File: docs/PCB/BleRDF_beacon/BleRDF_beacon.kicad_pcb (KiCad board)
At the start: 2 copper layers, 47 x 36 mm, 11 parts, among them J1 Conn_01x02, J2 Conn_01x02, J3 Conn_01x02, J4 Conn_01x02, U1 XIAO-ESP32-C6

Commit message: Update PCB wiring and add 3D case models
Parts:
- moved J4 20.6 mm to (58.0, 56.0)
- moved R3 6.13 mm to (63.0, 61.0), turned to 180 degrees
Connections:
- R3 pad 1: Net-(U1-GPIO20/D9/MISO) -> Net-(U1-GPIO17/D7/RX)
- U1 pad 10: Net-(U1-GPIO20/D9/MISO) -> unconnected-(U1-GPIO20/D9/MISO-Pad10)_1
- U1 pad 8: unconnected-(U1-GPIO17/D7/RX-Pad8)_1 -> Net-(U1-GPIO17/D7/RX)
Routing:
- net Net-(U1-GPIO20/D9/MISO): track 15.8 -> 0.00 mm
- net Net-(U1-GPIO17/D7/RX): track 0.00 -> 7.69 mm
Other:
- outline, holes or cut-outs redrawn
- board text added: "BleRDF Beacon v1.0"
- board text removed: "BleRDF Beacon"
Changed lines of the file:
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@@
 	(net 4 "Net-(U1-GPIO0{slash}A0{slash}D0)")
 	(net 5 "Net-(J2-Pin_2)")
-	(net 6 "Net-(U1-GPIO20{slash}D9{slash}MISO)")
+	(net 6 "Net-(U1-GPIO17{slash}D7{slash}RX)")
 	(net 7 "unconnected-(U1-GPIO19{slash}D8{slash}SCK-Pad9)")
 	(net 8 "unconnected-(U1-GPIO2{slash}A2{slash}D2-Pad3)")
@@
 	(net 13 "unconnected-(U1-GPIO22{slash}D4{slash}SDA-Pad5)")
 	(net 14 "unconnected-(U1-GPIO21{slash}D3-Pad4)_1")
-	(net 15 "unconnected-(U1-GPIO17{slash}D7{slash}RX-Pad8)")
+	(net 15 "unconnected-(U1-GPIO20{slash}D9{slash}MISO-Pad10)")
 	(net 16 "unconnected-(U1-GPIO18{slash}D10{slash}MOSI-Pad11)_1")
 	(net 17 "unconnected-(U1-GPIO19{slash}D8{slash}SCK-Pad9)_1")
@@
 	(net 23 "unconnected-(U1-GPIO23{slash}D5{slash}SCL-Pad6)_1")
 	(net 24 "unconnected-(U1-GPIO1{slash}A1{slash}D1-Pad2)_1")
-	(net 25 "unconnected-(U1-GPIO17{slash}D7{slash}RX-Pad8)_1")
+	(net 25 "unconnected-(U1-GPIO20{slash}D9{slash}MISO-Pad10)_1")
 	(net 26 "unconnected-(U1-GPIO22{slash}D4{slash}SDA-Pad5)_1")
 	(net 27 "VCC")
@@
 		(tags "CONN DEV")
 		(property "Reference" "F1"
-			(at -3 0.9 90)
+			(at 1.1 1.9 90)
 			(layer "F.SilkS")
 			(effects
@@
 		)
 		(fp_text user "${REFERENCE}"
-			(at 5 -0.91 90)
+			(at 1.25 0 90)
 			(layer "F.Fab")
 			(effects
@@
 	(footprint "Connector_JST:JST_XH_B2B-XH-A_1x02_P2.50mm_Vertical"
 		(layer "F.Cu")
-		(at 59.5 76.5 180)
+		(at 58 56 180)
 		(descr "JST XH series connector, B2B-XH-A (http://www.jst-mfg.com/product/pdf/eng/eXH.pdf), generated with kicad-footprint-generator")
 		(tags "connector JST XH vertical")
 		(property "Reference" "J4"
-			(at -1.5 5 0)
+			(at -4 -0.6 0)
 			(layer "F.SilkS")
 			(effects
@@
 	(footprint "Resistor_THT:R_Axial_DIN0204_L3.6mm_D1.6mm_P7.62mm_Horizontal"
 		(layer "F.Cu")
-		(at 57.5 63.69 -90)
+		(at 63.01 61 180)
 		(descr "Resistor, Axial_DIN0204 series, Axial, Horizontal, pin pitch=7.62mm, 0.167W, length*diameter=3.6*1.6mm^2, http://cdn-reichelt.de/documents/datenblatt/B400/1_4W%23YAG.pdf")
 		(tags "Resistor Axial_DIN0204 series Axial Horizontal pin pitch 7.62mm 0.167W length 3.6mm diameter 1.6mm")
 		(property "Reference" "R3"
-			(at 3.81 0 90)
+			(at 3.81 0 0)
 			(layer "F.SilkS")
 			(effects
@@
 		)
 		(property "Value" "1k"
-			(at 3.81 1.92 90)
+			(at 3.81 1.92 0)
 			(layer "F.Fab")
 			(hide yes)
@@
 		)
 		(property "Datasheet" "~"
-			(at 0 0 90)
+			(at 0 0 0)
 			(layer "F.Fab")
 			(hide yes)
@@
 		)
 		(property "Description" "Resistor"
-			(at 0 0 90)
+			(at 0 0 0)
 			(layer "F.Fab")
 			(hide yes)
@@
 		(attr through_hole)
 		(fp_line
-			(start 0.94 0)
-			(end 1.89 0)
+			(start 6.68 0)
+			(end 5.73 0)
 			(stroke
 				(width 0.12)
@@
 		)
 		(fp_line
-			(start 6.68 0)
-			(end 5.73 0)
+			(start 0.94 0)
+			(end 1.89 0)
 			(stroke
 				(width 0.12)
@@
 		)
 		(fp_line
-			(start 0 0)
-			(end 2.01 0)
+			(start 7.62 0)
+			(end 5.61 0)
 			(stroke
 				(width 0.1)
@@
 		)
 		(fp_line
-			(start 7.62 0)
-			(end 5.61 0)
+			(start 0 0)
+			(end 2.01 0)
 			(stroke
 				(width 0.1)
@@
 		)
 		(fp_text user "${REFERENCE}"
-			(at 3.81 0 90)
+			(at 3.81 0 0)
 			(layer "F.Fab")
 			(effects
@@
 		)
 		(pad "1" thru_hole circle
-			(at 0 0 270)
+			(at 0 0 180)
 			(size 1.4 1.4)
 			(drill 0.7)
 			(layers "*.Cu" "*.Mask")
 			(remove_unused_layers no)
-			(net 6 "Net-(U1-GPIO20{slash}D9{slash}MISO)")
+			(net 6 "Net-(U1-GPIO17{slash}D7{slash}RX)")
 			(pintype "passive")
 		)
 		(pad "2" thru_hole circle
-			(at 7.62 0 270)
+			(at 7.62 0 180)
 			(size 1.4 1.4)
 			(drill 0.7)
@@
 			(layers "*.Cu" "*.Mask")
 			(remove_unused_layers no)
-			(net 15 "unconnected-(U1-GPIO17{slash}D7{slash}RX-Pad8)")
+			(net 6 "Net-(U1-GPIO17{slash}D7{slash}RX)")
 			(pinfunction "GPIO17/D7/RX")
-			(pintype "passive+no_connect")
+			(pintype "passive")
 		)
 		(pad "8" smd roundrect
@@
 			(layers "F.Cu" "F.Mask")
 			(roundrect_rratio 0.1)
-			(net 25 "unconnected-(U1-GPIO17{slash}D7{slash}RX-Pad8)_1")
+			(net 6 "Net-(U1-GPIO17{slash}D7{slash}RX)")
 			(pinfunction "GPIO17/D7/RX")
-			(pintype "passive+no_connect")
+			(pintype "passive")
 			(thermal_bridge_angle 45)
 		)
@@
 			(layers "*.Cu" "*.Mask")
 			(remove_unused_layers no)
-			(net 6 "Net-(U1-GPIO20{slash}D9{slash}MISO)")
+			(net 15 "unconnected-(U1-GPIO20{slash}D9{slash}MISO-Pad10)")
 			(pinfunction "GPIO20/D9/MISO")
-			(pintype "passive")
+			(pintype "passive+no_connect")
 		)
 		(pad "10" smd roundrect
@@
 			(layers "F.Cu" "F.Mask")
 			(roundrect_rratio 0.1)
-			(net 6 "Net-(U1-GPIO20{slash}D9{slash}MISO)")
+			(net 25 "unconnected-(U1-GPIO20{slash}D9{slash}MISO-Pad10)_1")
 			(pinfunction "GPIO20/D9/MISO")
-			(pintype "passive")
+			(pintype "passive+no_connect")
 			(thermal_bridge_angle 45)
 		)
@@
 		(tags "connector JST XH vertical")
 		(property "Reference" "J3"
-			(at 5 -4.25 90)
+			(at 1.8 -3.6 90)
 			(layer "F.SilkS")
 			(effects
@@
 		(embedded_fonts no)
 	)
-	(gr_rect
-		(start 50 50)
-		(end 97 86)
+	(gr_line
+		(start 50 84)
+		(end 52 86)
+		(stroke
+			(width 0.2)
+			(type default)
+		)
+		(layer "Edge.Cuts")
+	)
+	(gr_line
+		(start 52 86)
+		(end 95 86)
+		(stroke
+			(width 0.2)
+			(type default)
+		)
+		(layer "Edge.Cuts")
+	)
+	(gr_line
+		(start 95 86)
+		(end 97 84)
+		(stroke
+			(width 0.2)
+			(type default)
+		)
+		(layer "Edge.Cuts")
+	)
+	(gr_line
+		(start 95 50)
+		(end 52 50)
+		(stroke
+			(width 0.2)
+			(type default)
+		)
+		(layer "Edge.Cuts")
+	)
+	(gr_line
+		(start 50 52)
+		(end 50 84)
+		(stroke
+			(width 0.2)
+			(type default)
+		)
+		(layer "Edge.Cuts")
+	)
+	(gr_line
+		(start 97 52)
+		(end 95 50)
+		(stroke
+			(width 0.2)
+			(type default)
+		)
+		(layer "Edge.Cuts")
+	)
+	(gr_line
+		(start 52 50)
+		(end 50 52)
+		(stroke
+			(width 0.2)
+			(type default)
+		)
+		(layer "Edge.Cuts")
+	)
+	(gr_line
+		(start 97 84)
+		(end 97 52)
 		(stroke
-			(width 0.05)
+			(width 0.2)
 			(type default)
 		)
-		(fill no)
 		(layer "Edge.Cuts")
 	)
-	(gr_text "BleRDF\nBeacon"
-		(at 51.25 84.25 0)
-		(layer "F.SilkS")
+	(gr_text "BleRDF\nBeacon v1.0"
+		(at 95.3 55.9 0)
+		(layer "B.SilkS")
 		(effects
 			(font
@@
 				(thickness 0.2)
 			)
-			(justify left bottom)
+			(justify left bottom mirror)
 		)
 	)
@@
 	)
 	(segment
-		(start 57.5 63.69)
-		(end 59.94 63.69)
-		(width 0.5)
-		(layer "F.Cu")
-		(net 6)
-	)
-	(segment
-		(start 61 64.75)
-		(end 61 71)
-		(width 0.5)
-		(layer "F.Cu")
-		(net 6)
-	)
-	(segment
-		(start 62.39 72.39)
-		(end 66.04 72.39)
-		(width 0.5)
-		(layer "F.Cu")
-		(net 6)
-	)
-	(segment
-		(start 59.94 63.69)
-		(end 61 64.75)
+		(start 63.01 64.28)
+		(end 66.04 67.31)
 		(width 0.5)
 		(layer "F.Cu")
@@
 	)
 	(segment
-		(start 61 71)
-		(end 62.39 72.39)
+		(start 63.01 61)
+		(end 63.01 64.28)
 		(width 0.5)
 		(layer "F.Cu")
@@
 		(width 0.5)
 		(layer "B.Cu")
-		(net 15)
+		(net 6)
 	)
 	(segment
@@
 	(segment
 		(start 63.01 80.01)
-		(end 66.04 80.01)
+		(end 59.5 76.5)
 		(width 0.5)
-		(layer "F.Cu")
+		(layer "B.Cu")
 		(net 28)
 	)
 	(segment
-		(start 59.5 76.5)
+		(start 66.04 80.01)
 		(end 63.01 80.01)
 		(width 0.5)
-		(layer "F.Cu")
+		(layer "B.Cu")
 		(net 28)
 	)
 	(segment
-		(start 57.5 71.31)
-		(end 57.5 76)
+		(start 55.5 56)
+		(end 55.5 60.89)
 		(width 0.5)
 		(layer "F.Cu")
@@
 	)
 	(segment
-		(start 57.5 76)
-		(end 57 76.5)
+		(start 55.5 60.89)
+		(end 55.39 61)
 		(width 0.5)
 		(layer "F.Cu")

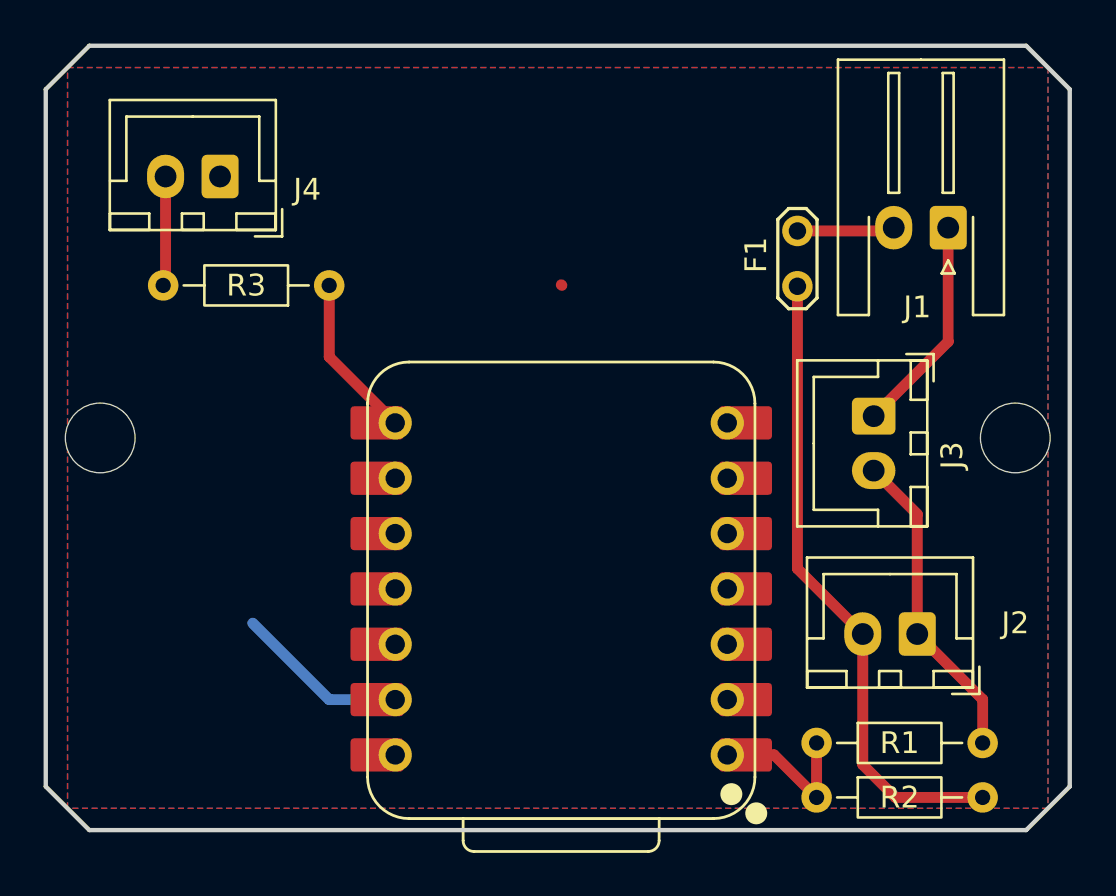
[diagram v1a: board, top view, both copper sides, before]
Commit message: Update 3D cases and pcb,hardware documentation
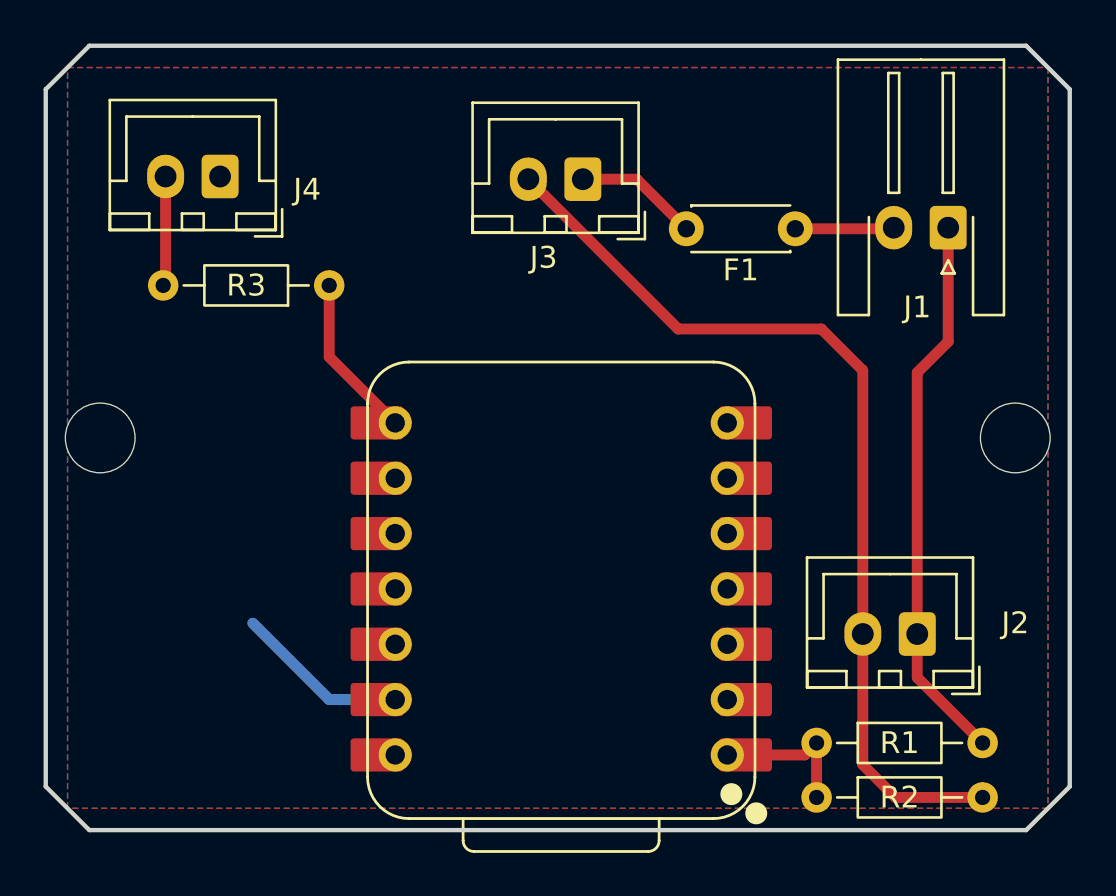
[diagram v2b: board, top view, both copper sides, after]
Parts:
- F1: footprint TestPoint:TestPoint_2Pads_Pitch2.54mm_Drill0.8mm -> Capacitor_THT:C_Disc_D4.3mm_W1.9mm_P5.00mm
- moved J3 17.2 mm to (74.7, 56.1), turned to 180 degrees
- moved F1 5.10 mm to (79.4, 58.4), turned to 0 degrees
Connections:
- F1 pad 1: Net-(J1-Pin_2) -> Net-(J3-Pin_1)
- F1 pad 2: Net-(J2-Pin_2) -> Net-(J1-Pin_2)
- J2 pad 1: Net-(J2-Pin_1) -> Net-(J1-Pin_1)
- J3 pad 1: Net-(J1-Pin_1) -> Net-(J3-Pin_1)
- J3 pad 2: Net-(J2-Pin_1) -> Net-(J2-Pin_2)
- R1 pad 2: Net-(J2-Pin_1) -> Net-(J1-Pin_1)
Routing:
- net Net-(J1-Pin_1): track 10.1 -> 25.5 mm
- net Net-(J2-Pin_1): track 14.6 -> 0.00 mm
- net Net-(J2-Pin_2): track 29.3 -> 43.2 mm
- net Net-(J3-Pin_1): track 0.00 -> 5.69 mm
- net Net-(U1-GPIO0/A0/D0): track 7.79 -> 7.21 mm
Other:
- board text added: "BleRDF Beacon V1.0"
- board text removed: "BleRDF Beacon v1.0"

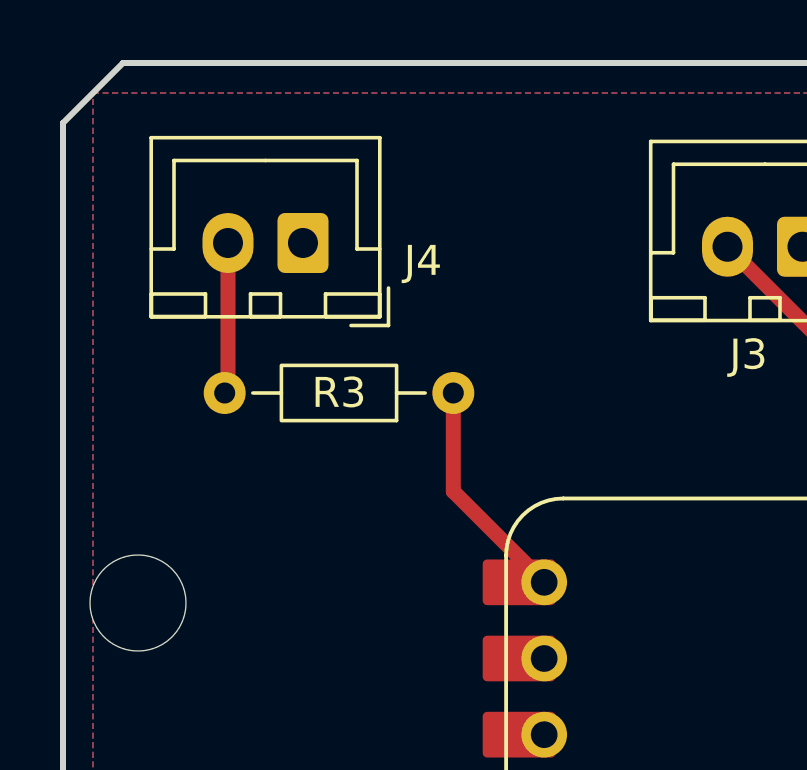
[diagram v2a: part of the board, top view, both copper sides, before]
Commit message: Fix LED Connector Directon BleRDF_Beacon PCB
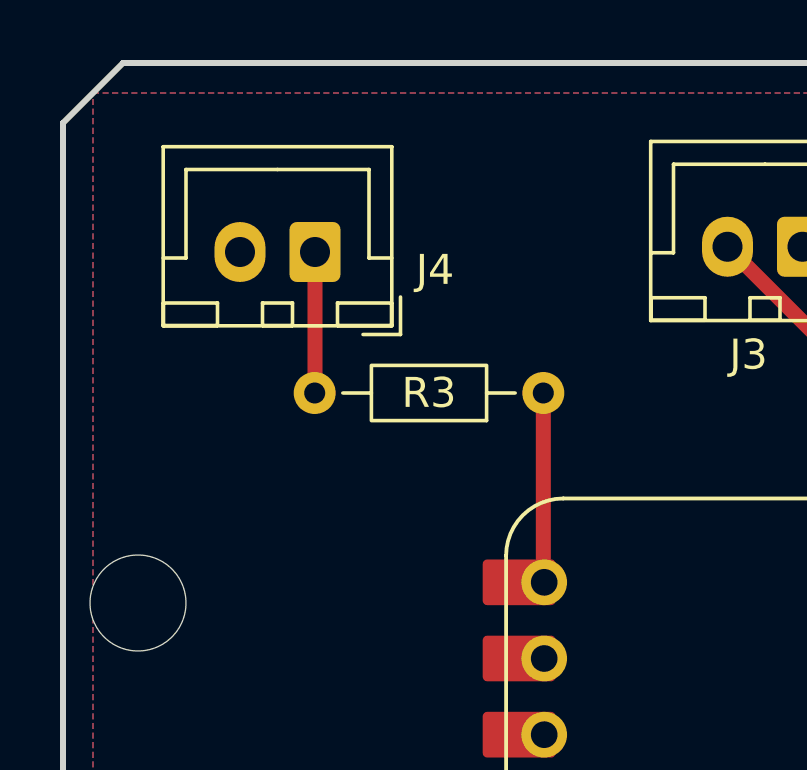
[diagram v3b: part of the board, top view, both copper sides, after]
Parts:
- moved R3 3.00 mm to (66.0, 61.0)
- moved J4 0.50 mm to (58.4, 56.3)
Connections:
- J4 pad 1: GND -> Net-(J4-Pin_1)
- J4 pad 2: Net-(J4-Pin_2) -> GND
- R3 pad 2: Net-(J4-Pin_2) -> Net-(J4-Pin_1)
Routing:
- net Net-(J4-Pin_2): track 5.05 -> 0.00 mm
- net Net-(J4-Pin_1): track 0.00 -> 4.70 mm
- net Net-(U1-GPIO17/D7/RX): track 7.69 -> 6.44 mm
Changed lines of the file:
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@@
 	(net 26 "VCC")
 	(net 27 "GND")
-	(net 28 "Net-(J4-Pin_2)")
+	(net 28 "Net-(J4-Pin_1)")
 	(net 29 "Net-(J3-Pin_1)")
 	(footprint "MountingHole:MountingHole_3.2mm_M3"
@@
 	(footprint "Connector_JST:JST_XH_B2B-XH-A_1x02_P2.50mm_Vertical"
 		(layer "F.Cu")
-		(at 58 56 180)
+		(at 58.4 56.3 180)
 		(descr "JST XH series connector, B2B-XH-A (http://www.jst-mfg.com/product/pdf/eng/eXH.pdf), generated with kicad-footprint-generator")
 		(tags "connector JST XH vertical")
@@
 			(remove_unused_layers no)
 			(roundrect_rratio 0.147059)
-			(net 27 "GND")
+			(net 28 "Net-(J4-Pin_1)")
 			(pinfunction "Pin_1")
 			(pintype "passive")
@@
 			(layers "*.Cu" "*.Mask")
 			(remove_unused_layers no)
-			(net 28 "Net-(J4-Pin_2)")
+			(net 27 "GND")
 			(pinfunction "Pin_2")
 			(pintype "passive")
@@
 	(footprint "Resistor_THT:R_Axial_DIN0204_L3.6mm_D1.6mm_P7.62mm_Horizontal"
 		(layer "F.Cu")
-		(at 63.01 61 180)
+		(at 66.01 61 180)
 		(descr "Resistor, Axial_DIN0204 series, Axial, Horizontal, pin pitch=7.62mm, 0.167W, length*diameter=3.6*1.6mm^2, http://cdn-reichelt.de/documents/datenblatt/B400/1_4W%23YAG.pdf")
 		(tags "Resistor Axial_DIN0204 series Axial Horizontal pin pitch 7.62mm 0.167W length 3.6mm diameter 1.6mm")
@@
 			(layers "*.Cu" "*.Mask")
 			(remove_unused_layers no)
-			(net 28 "Net-(J4-Pin_2)")
+			(net 28 "Net-(J4-Pin_1)")
 			(pintype "passive")
 		)
@@
 	)
 	(segment
-		(start 63.01 64.28)
+		(start 66.01 67.28)
 		(end 66.04 67.31)
 		(width 0.5)
@@
 	)
 	(segment
-		(start 63.01 61)
-		(end 63.01 64.28)
+		(start 66.01 61)
+		(end 66.01 67.28)
 		(width 0.5)
 		(layer "F.Cu")
@@
 	)
 	(segment
-		(start 55.5 56)
-		(end 55.5 60.89)
+		(start 58.4 56.3)
+		(end 58.4 60.99)
 		(width 0.5)
 		(layer "F.Cu")
@@
 	)
 	(segment
-		(start 55.5 60.89)
-		(end 55.39 61)
+		(start 58.4 60.99)
+		(end 58.39 61)
 		(width 0.5)
 		(layer "F.Cu")
